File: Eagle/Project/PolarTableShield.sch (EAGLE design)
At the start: 47 parts, among them IC1 74AHC1G86DBV, IC2 LM358D, J1 Pi Power Jack, J10 LED + Radio, J2 Header - Right angled, female, J3 Pi Connection, J5 IR Sensors, J6 Switch A + B, J7 Switch C + D, J8 Switch E + F, Q1 BC337, Q2 2N3906, Q3 BC547, Q4 2N7000, Q5 2N7000, U3 SN74HC595DR

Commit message: Moved the pins to be more efficient.
Put the rotory encoder signals onto D8 & D9 so they are on digital pin bank B in the lowest two bits. This can save a cycle shifting the data into position.
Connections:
- net D11_SDIN renamed SDIN
- net D12_RXDATA renamed RXDATA
- net D13_SCIN renamed SCIN
- removed net A0_SW_E: B1.A0, IC1A.I0, J8.3
- removed net A1_SW_F: B1.A1, IC1A.I1, J8.4
- removed net A2_WAKE_SW: B1.*D3, B1.A2, IC1A.O, J10.3, JP3.1
- new net SW_E: B1.D8, IC1A.I0, J8.3
- new net SW_F: B1.*D9, IC1A.I1, J8.4
- new net WAKE_SW: B1.*D10, B1.*D3, IC1A.O, J10.3, JP3.1
- net CLK: now also B1.A1; no longer B1.*D10
- net DATA: now also B1.A0; no longer B1.*D9
- net LATCH: now also B1.A2; no longer B1.D8
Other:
- note removed: "WIP: OR gate for interupts"
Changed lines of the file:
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@@
 </classes>
 <parts>
-<part name="B1" library="keir_library" deviceset="ARDUINO_UNO_R3_SHIELD" device="NOLABELS" package3d_urn="urn:adsk.eagle:package:37324/1" value=""/>
+<part name="B1" library="keir_library" deviceset="ARDUINO_UNO_R3_SHIELD" device="NOLABELS" package3d_urn="urn:adsk.eagle:package:37324/1" value="ARDUINO_UNO_R3_SHIELDNOLABELS"/>
 <part name="J1" library="SparkFun-Connectors" library_urn="urn:adsk.eagle:library:513" deviceset="POWER_JACK" device="PTH_BREAD" package3d_urn="urn:adsk.eagle:package:38228/1" value="Pi Power Jack"/>
 <part name="J2" library="keir_library" deviceset="CONN_03" device="1X03_2.54MM_RA_FEMALE" package3d_urn="urn:adsk.eagle:package:38063/1" value="Header - Right angled, female"/>
@@
 <part name="Q1" library="transistor-npn" library_urn="urn:adsk.eagle:library:398" deviceset="BC337*" device="" package3d_urn="urn:adsk.eagle:package:28523/2"/>
 <part name="R1" library="rcl" library_urn="urn:adsk.eagle:library:334" deviceset="R-EU_" device="M0805" package3d_urn="urn:adsk.eagle:package:23556/1" value="1k"/>
-<part name="B2" library="keir_library" deviceset="ARDUINO_UNO_R3_SHIELD" device="NOLABELS" package3d_urn="urn:adsk.eagle:package:37324/1" value=""/>
+<part name="B2" library="keir_library" deviceset="ARDUINO_UNO_R3_SHIELD" device="NOLABELS" package3d_urn="urn:adsk.eagle:package:37324/1" value="ARDUINO_UNO_R3_SHIELDNOLABELS"/>
 <part name="C4" library="resistor" library_urn="urn:adsk.eagle:library:348" deviceset="C-EU" device="C0805" package3d_urn="urn:adsk.eagle:package:23617/2" value="100nF"/>
 <part name="C5" library="resistor" library_urn="urn:adsk.eagle:library:348" deviceset="C-EU" device="C0805" package3d_urn="urn:adsk.eagle:package:23617/2" value="330uF"/>
@@
 <text x="127" y="177.8" size="1.9304" layer="95" font="vector">Open JP3 to disable
 hard reset.</text>
-<text x="96.52" y="152.4" size="1.9304" layer="95" font="vector">WIP: OR gate for interupts</text>
 </plain>
 <instances>
@@
 </segment>
 </net>
-<net name="A2_WAKE_SW" class="4">
+<net name="WAKE_SW" class="4">
 <segment>
 <label x="322.58" y="215.9" size="1.27" layer="95" rot="MR0" xref="yes"/>
@@
 </segment>
 <segment>
-<label x="78.74" y="172.72" size="1.27" layer="95" rot="MR180" xref="yes"/>
-<pinref part="B1" gate="G$1" pin="A2"/>
-<wire x1="78.74" y1="172.72" x2="71.12" y2="172.72" width="0.1524" layer="91"/>
+<label x="40.64" y="149.86" size="1.27" layer="95" rot="MR0" xref="yes"/>
+<pinref part="B1" gate="G$1" pin="*D10"/>
+<wire x1="40.64" y1="149.86" x2="45.72" y2="149.86" width="0.1524" layer="91"/>
 </segment>
 <segment>
@@
 </segment>
 <segment>
-<pinref part="B1" gate="G$1" pin="*D10"/>
-<wire x1="45.72" y1="149.86" x2="40.64" y2="149.86" width="0.1524" layer="91"/>
-<label x="40.64" y="149.86" size="1.27" layer="95" rot="MR0" xref="yes"/>
+<pinref part="B1" gate="G$1" pin="A1"/>
+<wire x1="71.12" y1="175.26" x2="78.74" y2="175.26" width="0.1524" layer="91"/>
+<label x="78.74" y="175.26" size="1.27" layer="95" rot="MR180" xref="yes"/>
 </segment>
 </net>
@@
 </segment>
 <segment>
-<pinref part="B1" gate="G$1" pin="D8"/>
-<wire x1="45.72" y1="154.94" x2="40.64" y2="154.94" width="0.1524" layer="91"/>
-<label x="40.64" y="154.94" size="1.27" layer="95" rot="MR0" xref="yes"/>
+<pinref part="B1" gate="G$1" pin="A2"/>
+<wire x1="71.12" y1="172.72" x2="78.74" y2="172.72" width="0.1524" layer="91"/>
+<label x="78.74" y="172.72" size="1.27" layer="95" rot="MR180" xref="yes"/>
 </segment>
 </net>
@@
 </segment>
 <segment>
-<pinref part="B1" gate="G$1" pin="*D9"/>
-<wire x1="45.72" y1="152.4" x2="40.64" y2="152.4" width="0.1524" layer="91"/>
-<label x="40.64" y="152.4" size="1.27" layer="95" rot="MR0" xref="yes"/>
-</segment>
-</net>
-<net name="D12_RXDATA" class="4">
+<pinref part="B1" gate="G$1" pin="A0"/>
+<wire x1="71.12" y1="177.8" x2="78.74" y2="177.8" width="0.1524" layer="91"/>
+<label x="78.74" y="177.8" size="1.27" layer="95" rot="MR180" xref="yes"/>
+</segment>
+</net>
+<net name="RXDATA" class="4">
 <segment>
 <wire x1="342.9" y1="215.9" x2="350.52" y2="215.9" width="0.1524" layer="91"/>
@@
 </segment>
 </net>
-<net name="D13_SCIN" class="4">
+<net name="SCIN" class="4">
 <segment>
 <pinref part="B1" gate="G$1" pin="D13"/>
@@
 </segment>
 </net>
-<net name="A0_SW_E" class="4">
-<segment>
-<pinref part="B1" gate="G$1" pin="A0"/>
-<wire x1="71.12" y1="177.8" x2="78.74" y2="177.8" width="0.1524" layer="91"/>
-<label x="78.74" y="177.8" size="1.27" layer="95" xref="yes"/>
+<net name="SW_E" class="4">
+<segment>
+<pinref part="B1" gate="G$1" pin="D8"/>
+<wire x1="45.72" y1="154.94" x2="40.64" y2="154.94" width="0.1524" layer="91"/>
+<label x="40.64" y="154.94" size="1.27" layer="95" rot="R180" xref="yes"/>
 </segment>
 <segment>
@@
 </segment>
 </net>
-<net name="A1_SW_F" class="4">
-<segment>
-<pinref part="B1" gate="G$1" pin="A1"/>
-<wire x1="71.12" y1="175.26" x2="78.74" y2="175.26" width="0.1524" layer="91"/>
-<label x="78.74" y="175.26" size="1.27" layer="95" xref="yes"/>
+<net name="SW_F" class="4">
+<segment>
+<pinref part="B1" gate="G$1" pin="*D9"/>
+<wire x1="45.72" y1="152.4" x2="40.64" y2="152.4" width="0.1524" layer="91"/>
+<label x="40.64" y="152.4" size="1.27" layer="95" rot="R180" xref="yes"/>
 </segment>
 <segment>
@@
 </segment>
 </net>
-<net name="D11_SDIN" class="0">
+<net name="SDIN" class="0">
 <segment>
 <pinref part="B1" gate="G$1" pin="*D11"/>

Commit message: Remove the Arduino headers and just integrated the atmega328 directly
Added atmega328 chip
More indicator lights
Added 3.3v supply
ICP and SPI headers
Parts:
- removed B1: ARDUINO_UNO_R3_SHIELDNOLABELS, keir_library:ARDUINO_UNO_R3_SHIELDNOLABELS
- added C11, C12: 0.1uF, SparkFun:CAP0603-CAP
- added D2: Green, led:LEDCHIP-LED0805
- added IC3: LM340MP-05, linear:LM340MP-05
- added J11: Programmer, keir_library:CONN_03X2NO_SILK
- added J9: ISP, keir_library:CONN_03X2NO_SILK
- added Q7: 16MHz, Testing:RESONATOR1:1
- added R20: 10K, SparkFun:RESISTOR0603-RES
- added R21: 330, SparkFun:RESISTOR0603-RES
- added U4: ATMEGA328, SparkFun:ATMEGA168
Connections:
- removed net 3.3V: B1.3.3V, B2.3.3V, J10.6, J4.3, J5.11, J5.2, J6.5, J6.6, J7.5, J7.6, J8.5, J8.6, Q4.G, Q5.G, R11.1, R12.1, U$1G$1.3.3V
- removed net 5V: B1.5V, B2.5V, IC2P.V+, J5.12, Q2.E, R10.1, R14.1, R4.2, R6.1, R8.1, R9.1, U3.!SRCLR, U3.VCC
- removed net 5V_SUPPLY: C2.+, J2.3, J3.1, LED1.A
- removed net N$6: C1.-, C2.-, C9.2, J1.GND, J1.GNDBREAK, J2.2, R13.2
- removed net RX: B1.RX, B2.RX
- removed net RXDATA: B1.D12, J10.4
- removed net SCIN: B1.D13, J10.5
- removed net SDIN: B1.*D11, J10.7
- removed net TX: B1.TX, B2.TX
- new net A6: U4.ADC6
- new net A7: U4.ADC7
- new net MISO(RXDATA): J10.4, J9.1, U4.PB4(MISO)
- new net MOSI(SDIN): J10.7, J9.4, U4.PB3(MOSI/OC2)
- new net N$14: D2.A, R21.2
- new net N$15: Q7.3, U4.PB7(XTAL2/TOSC2)
- new net N$16: Q7.1, U4.PB6(XTAL1/TOSC1)
- new net RESET: J11.5, J9.5, R20.1, U4.PC6(/RESET)
- new net RXI: J11.1, U4.PD0(RXD)
- new net SCK(SCIN): J10.5, J9.3, R21.1, U4.PB5(SCK)
- new net TXO: J11.3, U4.PD1(TXD)
- new net VCC_1: B2.5V, C11.2, C2.+, IC2P.V+, IC3.VI, J11.2, J2.3, J3.1, J5.12, J9.2, LED1.A, Q2.E, R10.1, R14.1, R20.2, R4.2, R6.1, R8.1, R9.1, U3.!SRCLR, U3.VCC, U4.AVCC, U4.VCC@1, U4.VCC@2
- new net VCC_2: IC3.VO, J10.6, J4.3, J5.11, J5.2, J6.5, J6.6, J7.5, J7.6, J8.5, J8.6, Q4.G, Q5.G, R11.1, R12.1, U$1G$1.3.3V
- net !INT: now also U4.PD2(INT0); no longer B1.D2
- net !RES: no longer B1.RES
- net 12V_SUPPLY: no longer B1.VIN, B2.VIN
- net AREF: now also C12.2, U4.AREF; no longer B1.AREF, B2.AREF
- net CLK: now also U4.PC1(ADC1); no longer B1.A1
- net DATA: now also U4.PC0(ADC0); no longer B1.A0
- net GND: now also C1.-, C11.1, C12.1, C2.-, C9.2, D2.C, IC3.GND, J1.GND, J1.GNDBREAK, J11.6, J2.2, J9.6, Q7.2, R13.2, U4.AGND, U4.GND@1, U4.GND@2; no longer B1.GND@0, B1.GND@1, B1.GND@2
- net IOREF: no longer B1.IOREF
- net LATCH: now also U4.PC2(ADC2); no longer B1.A2
- net PIPOWER_SIGNAL: now also U4.PC3(ADC3); no longer B1.A3
- net SCL: now also U4.PC5(ADC5/SCL); no longer B1.A5, B1.SCL, B2.A5, B2.SCL
- net SDA: now also U4.PC4(ADC4/SDA); no longer B1.A4, B1.SDA, B2.A4, B2.SDA
- net SW_E: now also IC1A.I1, U4.PB0(ICP); no longer B1.D8, IC1A.I0
- net SW_F: now also IC1A.I0, U4.PB1(OC1A); no longer B1.*D9, IC1A.I1
- net WAKE_SW: now also U4.PB2(SS/OC1B), U4.PD3(INT1); no longer B1.*D10, B1.*D3
- net XDIR: now also U4.PD7(AIN1); no longer B1.D7
- net XSTEP: now also U4.PD6(AIN0); no longer B1.*D6
- net YDIR: now also U4.PD5(T1); no longer B1.*D5
- net YSTEP: now also U4.PD4(XCK/T0); no longer B1.D4
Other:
- note added: "Arduino"
- note added: "Combine the switch and Encoder Interupts"
- note removed: "Headers down to Arduino"
- moved on the sheet: B2, IC1, LED2

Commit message: Updates to the interrupt logic
The timer button and the relative encoder signals now OR together.
The relative encoder now has an XORed interrupt  trigger.
Replaced the main diode with something a bit smaller.
Replaced the 3.3v regulator chip.
Added buffers to the encoder signals.
Changed the crystal setup on the atmega chip.
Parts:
- removed D1: 1N5408, keir_library:1N5408
- removed IC1: 74AHC1G86DBV, 74xx-little-us:74AHC1G86DBV
- removed IC3: LM340MP-05, linear:LM340MP-05
- removed Q7: 16MHz, Testing:RESONATOR1:1
- added C3, C6: 13pF, SparkFun:CAP0603-CAP
- added D3: (no value), diode:SCHOTTKY-DIODESMD
- added U1: XOR, Texas Instruments - SN74LVC1G58:TEXAS_INSTRUMENTS_SN74LVC1G58SOT363
- added U2: OR, Texas Instruments - SN74LVC1G58:TEXAS_INSTRUMENTS_SN74LVC1G58SOT363
- added U5, U6, U7: Buffer, Texas Instruments - SN74LVC1G58:TEXAS_INSTRUMENTS_SN74LVC1G58SOT363
- added U8: CD74HC4094M96, keir_library:CD74HC4094M96
- added Y1: TSX-3225_16.0000MF18X-AC3, keir_library:TSX-3225_16.0000MF18X-AC3
- Q3: value BC547 -> 2N3904; device transistor-npn:BC547 -> transistor-npn:2N3904
- R3: value 22k -> 47k
- R4: value 16.2k -> 3k
- R5: value 221k -> 11k
- R9: value 1k -> 5k
- U3: value SN74HC595DR -> TLV73333PDBVT; device keir_library:SN74HC595HCD -> keir_library:TLV73333PDBVT
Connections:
- removed net CLK: U3.SERCLK, U4.PC1(ADC1)
- removed net N$15: Q7.3, U4.PB7(XTAL2/TOSC2)
- new net CLOCK: U4.PC1(ADC1), U8.CP
- new net N$6: R9.1, VR1.CCW
- new net SW_EF_XOR: U1.Y, U2.C
- new net SW_E_BUF: U1.C, U4.PB0(ICP), U6.Y
- new net SW_F_BUF: U1.A, U1.B, U4.PB1(OC1A), U5.Y
- new net SW_OR_ENCODER: U2.Y, U4.PD3(INT1)
- new net WAKE_SW_BUF: JP3.1, U2.A, U4.PB2(SS/OC1B), U7.Y
- net !RES: now also Q3.C; no longer Q3.E
- net 12V_SUPPLY: now also D3.C; no longer D1.C
- net DATA: now also U8.DATA; no longer U3.SER
- net ENX: now also U8.Q1; no longer U3.B
- net ENY: now also U8.Q3; no longer U3.D
- net GND: now also C3.2, C6.2, Q3.E, U1.GND, U2.B, U2.GND, U5.B, U5.C, U5.GND, U6.B, U6.C, U6.GND, U7.B, U7.C, U7.GND, Y1.GND; no longer IC3.GND, Q7.2, U3.!OE
- net LATCH: now also U8.STROBE; no longer U3.RCLK
- net N$16: now also C6.1, Y1.3; no longer Q7.1
- net N$3: now also Q2.C; no longer Q3.C
- net N$4: now also D3.A; no longer D1.A
- net N$7: now also C3.1, U4.PB7(XTAL2/TOSC2), Y1.1; no longer Q2.C, VR1.CCW
- net SLEEPX: now also U8.Q0; no longer U3.A
- net SLEEPY: now also U8.Q2; no longer U3.C
- net SW_E: now also U6.A; no longer IC1A.I1, U4.PB0(ICP)
- net SW_F: now also U5.A; no longer IC1A.I0, U4.PB1(OC1A)
- net VCC_1: now also U1.VCC, U2.VCC, U3.EN, U3.IN, U5.VCC, U6.VCC, U7.VCC, U8.VCC; no longer IC3.VI, R9.1, U3.!SRCLR, U3.VCC
- net VCC_2: now also B2.3.3V, U3.OUT; no longer IC3.VO
- net WAKE_SW: now also U7.A; no longer IC1A.O, JP3.1, U4.PB2(SS/OC1B), U4.PD3(INT1)
- net XMS1: now also U8.Q6; no longer U3.G
- net XMS2: now also U8.Q7; no longer U3.H
- net YMS1: now also U8.Q4; no longer U3.E
- net YMS2: now also U8.Q5; no longer U3.F
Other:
- moved on the sheet: C12, C5, IC2A, JP3, Q2, R2, R3, R4, R5, R7, R8, R9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

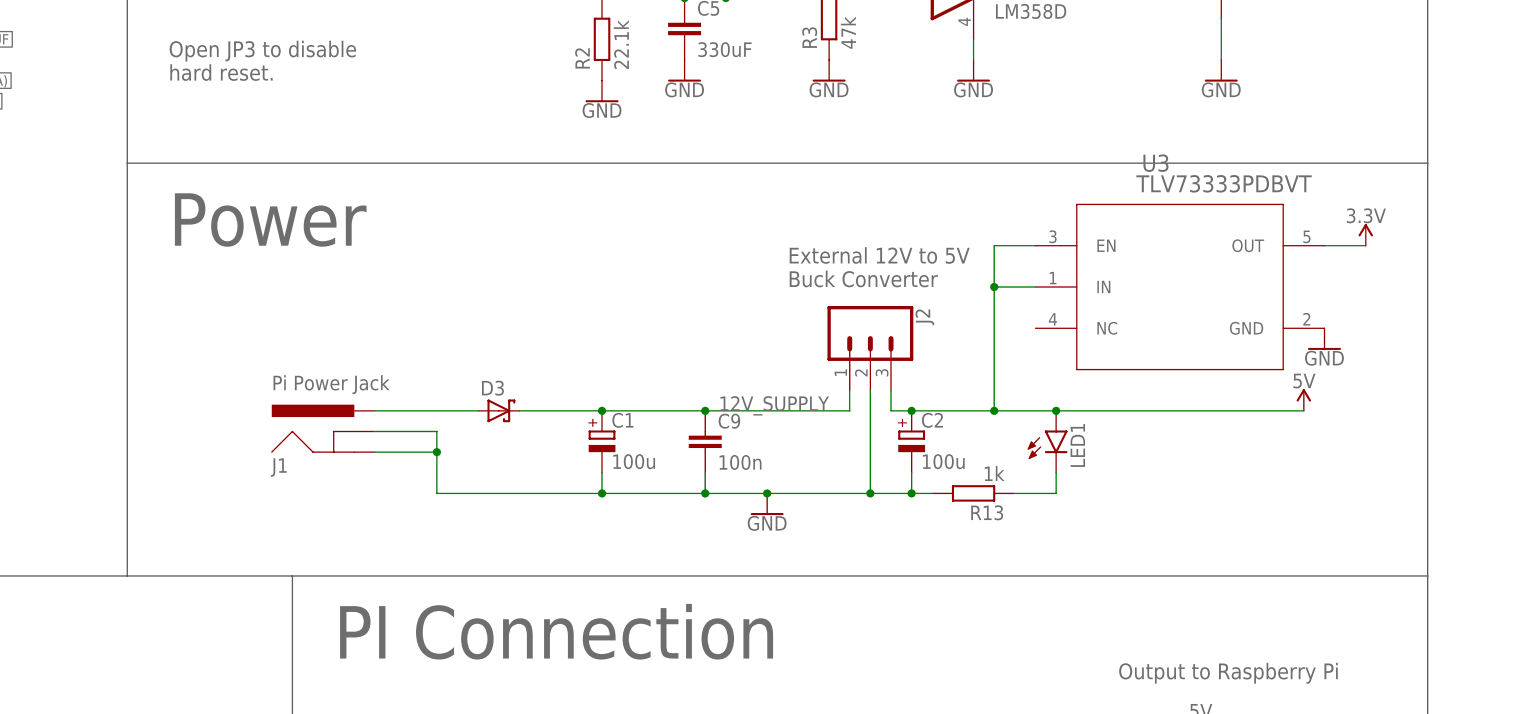
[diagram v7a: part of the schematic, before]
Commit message: Thinking about splitting out the power into a separate board.
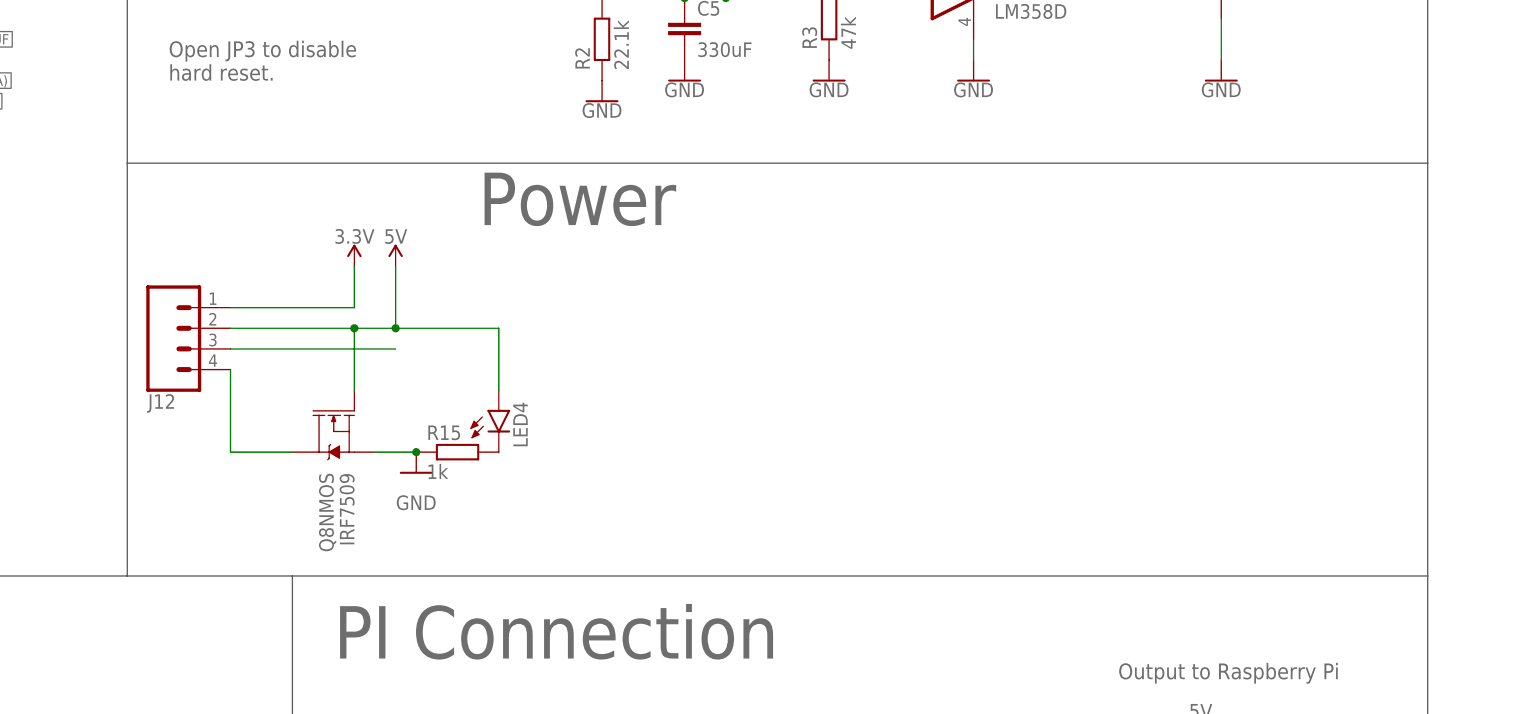
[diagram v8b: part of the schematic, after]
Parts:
- removed C1, C2: 100u, rcl:CPOL-EUE2-5
- removed C9: 100n, rcl:C-EUC0805
- removed D3: (no value), diode:SCHOTTKY-DIODESMD
- removed J1: Pi Power Jack, SparkFun-Connectors:POWER_JACKPTH_BREAD
- removed J2: Header - Right angled, female, keir_library:CONN_031X03_2.54MM_RA_FEMALE
- removed LED1: (no value), led:LEDCHIP-LED0805
- removed R13: 1k, rcl:R-EU_M0805
- removed U3: TLV73333PDBVT, keir_library:TLV73333PDBVT
- added J12: (no value), SparkFun-Connectors:CONN_04JST-PTH
- added LED4: (no value), led:LEDCHIP-LED0805
- added Q8: IRF7509, SparkFun-DiscreteSemi:IRF7509
- added R15: 1k, rcl:R-EU_M0805
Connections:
- net 12V_SUPPLY: now also J12.3; no longer C1.+, C9.1, D3.C, J2.1
- net GND: now also Q8NMOS.S, R15.1; no longer C1.-, C2.-, C9.2, J1.GND, J1.GNDBREAK, J2.2, R13.2, U3.GND
- net N$4: now also J12.4, Q8NMOS.D; no longer D3.A, J1.PWR
- net N$9: now also LED4.C, R15.2; no longer LED1.C, R13.1
- net VCC_1: now also J12.2, LED4.A, Q8NMOS.G; no longer C2.+, J2.3, LED1.A, U3.EN, U3.IN
- net VCC_2: now also J12.1; no longer U3.OUT
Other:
- note removed: "External 12V to 5V Buck Converter"
